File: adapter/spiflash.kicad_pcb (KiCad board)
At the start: 2 copper layers, 35 x 22 mm, 45 parts, among them J1 USB_C_Receptacle_USB2.0, J2 Tag-Connect, J3 Conn_01x02, J4 Conn_01x03, J5 Clip, U1 XC6206, U2 SRV05-4-P-T7, U4 STM32F103C8T6, U5 SN74LVC1T45DBV, U6 SN74LVC1T45DBV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

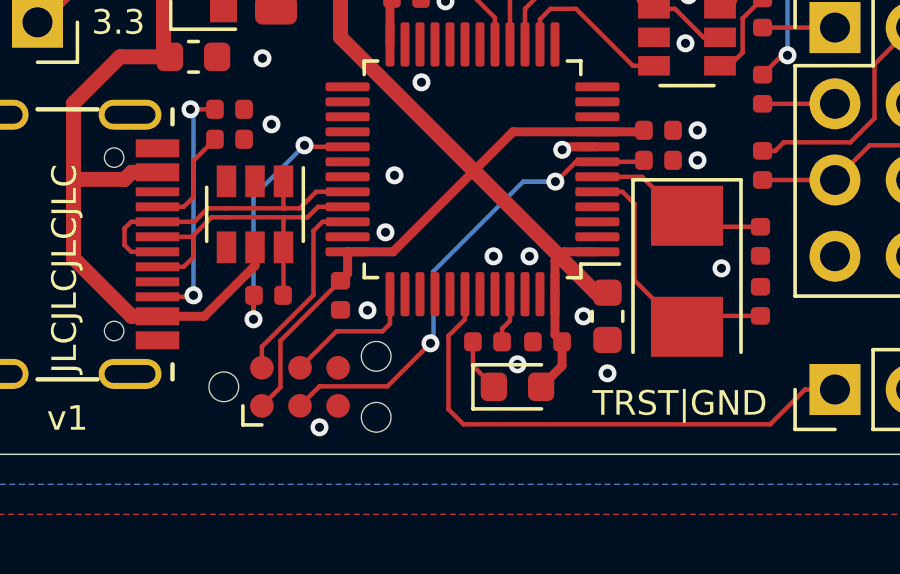
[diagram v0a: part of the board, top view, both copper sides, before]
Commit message: remap TRST
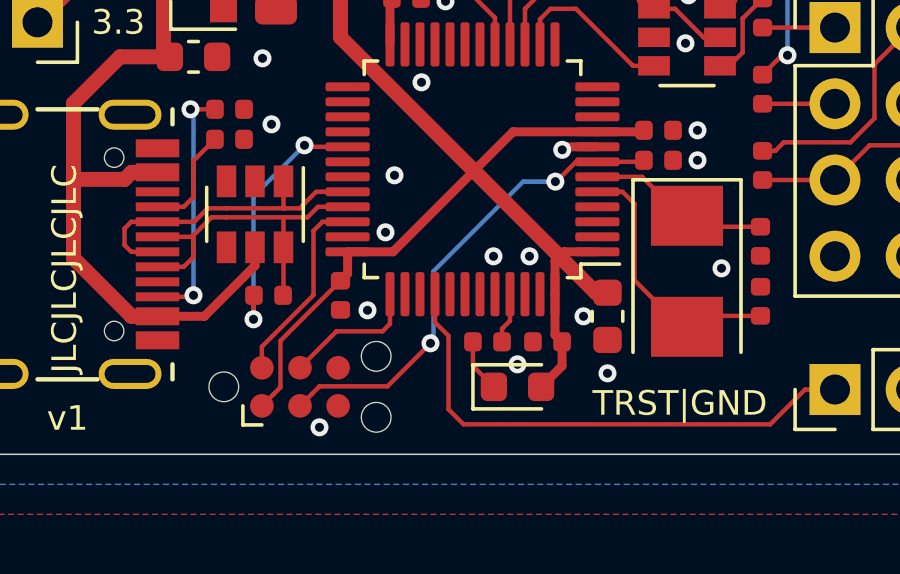
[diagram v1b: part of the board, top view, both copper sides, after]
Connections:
- U4 pad 40: Net-(U4-Pad40) -> /TRST
- U4 pad 42: /TRST -> Net-(U4-Pad42)

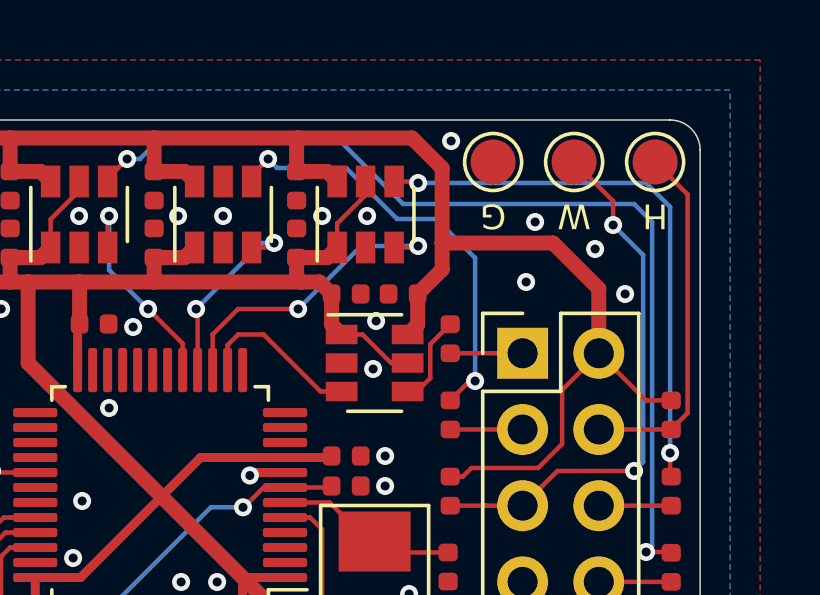
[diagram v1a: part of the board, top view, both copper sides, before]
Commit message: adapter: add Vtarget decoupling
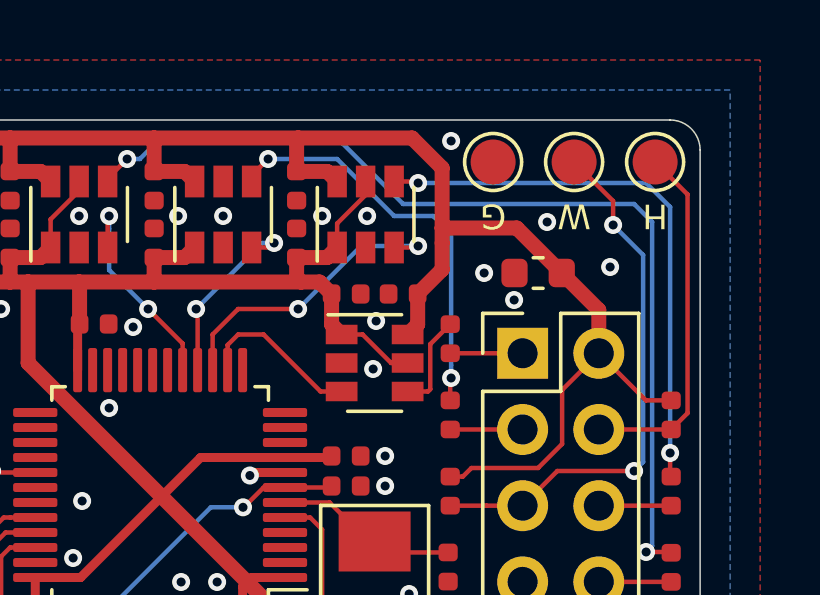
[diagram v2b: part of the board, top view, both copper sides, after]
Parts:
- added C5: 1u, Capacitor_SMD:C_0603_1608Metric, F.Cu at (129.6, 83.1)
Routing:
- net /MISO: track 14.4 -> 13.7 mm
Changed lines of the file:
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@@
     (thickness 1.6)
     (drawings 21)
-    (tracks 329)
+    (tracks 331)
     (zones 0)
-    (modules 45)
+    (modules 46)
     (nets 61)
   )
@@
     (add_net VBUS)
   )
+  (module Capacitor_SMD:C_0603_1608Metric (layer F.Cu)
+    (at 129.6 83.1 180)
+    (descr "Capacitor SMD 0603 (1608 Metric), square (rectangular) end terminal, IPC_7351 nominal, (Body size source: http://www.tortai-tech.com/upload/download/2011102023233369053.pdf), generated with kicad-footprint-generator")
+    (tags capacitor)
+    (attr smd)
+    (fp_text reference C5 (at 0 -1.43) (layer F.SilkS) hide
+      (effects (font (size 1 1) (thickness 0.15)))
+    )
+    (fp_text value 1u (at 0 1.43) (layer F.Fab)
+      (effects (font (size 1 1) (thickness 0.15)))
+    )
+    (fp_text user %R (at 0 0) (layer F.Fab)
+      (effects (font (size 0.4 0.4) (thickness 0.06)))
+    )
+    (fp_line (start 1.48 0.73) (end -1.48 0.73) (layer F.CrtYd) (width 0.05))
+    (fp_line (start 1.48 -0.73) (end 1.48 0.73) (layer F.CrtYd) (width 0.05))
+    (fp_line (start -1.48 -0.73) (end 1.48 -0.73) (layer F.CrtYd) (width 0.05))
+    (fp_line (start -1.48 0.73) (end -1.48 -0.73) (layer F.CrtYd) (width 0.05))
+    (fp_line (start -0.162779 0.51) (end 0.162779 0.51) (layer F.SilkS) (width 0.12))
+    (fp_line (start -0.162779 -0.51) (end 0.162779 -0.51) (layer F.SilkS) (width 0.12))
+    (fp_line (start 0.8 0.4) (end -0.8 0.4) (layer F.Fab) (width 0.1))
+    (fp_line (start 0.8 -0.4) (end 0.8 0.4) (layer F.Fab) (width 0.1))
+    (fp_line (start -0.8 -0.4) (end 0.8 -0.4) (layer F.Fab) (width 0.1))
+    (fp_line (start -0.8 0.4) (end -0.8 -0.4) (layer F.Fab) (width 0.1))
+    (pad 2 smd roundrect (at 0.7875 0 180) (size 0.875 0.95) (layers F.Cu F.Paste F.Mask) (roundrect_rratio 0.25)
+      (net 1 GND))
+    (pad 1 smd roundrect (at -0.7875 0 180) (size 0.875 0.95) (layers F.Cu F.Paste F.Mask) (roundrect_rratio 0.25)
+      (net 6 /V_TARGET))
+    (model ${KISYS3DMOD}/Capacitor_SMD.3dshapes/C_0603_1608Metric.wrl
+      (at (xyz 0 0 0))
+      (scale (xyz 1 1 1))
+      (rotate (xyz 0 0 0))
+    )
+  )
   (module Package_TO_SOT_SMD:SOT-23 (layer F.Cu)
     (at 107.7 84.25 180)
@@
   (via (at 124.5 89.2) (size 0.6) (drill 0.3) (layers F.Cu B.Cu) (net 1))
   (via (at 124.5 90.2) (size 0.6) (drill 0.3) (layers F.Cu B.Cu) (net 1))
-  (via (at 131.5 82.3) (size 0.6) (drill 0.3) (layers F.Cu B.Cu) (net 1))
-  (via (at 132.5 83.8) (size 0.6) (drill 0.3) (layers F.Cu B.Cu) (net 1))
-  (via (at 129.5 81.4) (size 0.6) (drill 0.3) (layers F.Cu B.Cu) (net 1))
-  (via (at 129.2 83.4) (size 0.6) (drill 0.3) (layers F.Cu B.Cu) (net 1))
   (via (at 126.7 78.7) (size 0.6) (drill 0.3) (layers F.Cu B.Cu) (net 1))
   (via (at 121.5 97.3) (size 0.6) (drill 0.3) (layers F.Cu B.Cu) (net 1))
+  (via (at 127.8 83.1) (size 0.6) (drill 0.3) (layers F.Cu B.Cu) (net 1))
+  (via (at 128.8 84) (size 0.6) (drill 0.3) (layers F.Cu B.Cu) (net 1))
+  (via (at 132 82.9) (size 0.6) (drill 0.3) (layers F.Cu B.Cu) (net 1))
+  (via (at 129.9 81.4) (size 0.6) (drill 0.3) (layers F.Cu B.Cu) (net 1))
   (segment (start 106.5 90.6) (end 105.638002 90.6) (width 0.5) (layer F.Cu) (net 2))
   (segment (start 109.75 93.712124) (end 109.75 93.1) (width 0.3) (layer F.Cu) (net 2))
@@
   (segment (start 121.6 78.6) (end 121.55 78.65) (width 0.5) (layer F.Cu) (net 6))
   (segment (start 121.6 78.6) (end 125.4 78.6) (width 0.5) (layer F.Cu) (net 6))
-  (segment (start 126.4 79.6) (end 126.4 82.1) (width 0.5) (layer F.Cu) (net 6))
   (segment (start 126.4 82.1) (end 126.4 82.985) (width 0.5) (layer F.Cu) (net 6))
-  (segment (start 131.623 85.776) (end 131.623 83.623) (width 0.5) (layer F.Cu) (net 6))
-  (segment (start 130.1 82.1) (end 126.4 82.1) (width 0.5) (layer F.Cu) (net 6))
-  (segment (start 131.623 83.623) (end 130.1 82.1) (width 0.5) (layer F.Cu) (net 6))
   (segment (start 130.4 86.999) (end 131.623 85.776) (width 0.15) (layer F.Cu) (net 6))
   (segment (start 127.09 89.886) (end 127.376 89.6) (width 0.15) (layer F.Cu) (net 6))
@@
   (segment (start 129.6 89.6) (end 130.4 88.8) (width 0.15) (layer F.Cu) (net 6))
   (segment (start 130.4 88.8) (end 130.4 86.999) (width 0.15) (layer F.Cu) (net 6))
+  (segment (start 131.623 84.3355) (end 130.3875 83.1) (width 0.5) (layer F.Cu) (net 6))
+  (segment (start 131.623 85.776) (end 131.623 84.3355) (width 0.5) (layer F.Cu) (net 6))
+  (segment (start 128.8875 81.6) (end 126.4 81.6) (width 0.5) (layer F.Cu) (net 6))
+  (segment (start 130.3875 83.1) (end 128.8875 81.6) (width 0.5) (layer F.Cu) (net 6))
+  (segment (start 126.4 79.6) (end 126.4 81.6) (width 0.5) (layer F.Cu) (net 6))
+  (segment (start 126.4 81.6) (end 126.4 82.1) (width 0.5) (layer F.Cu) (net 6))
   (segment (start 123.95 92.05) (end 124.15 92.05) (width 0.15) (layer F.Cu) (net 7))
   (segment (start 122.65 90.75) (end 123.95 92.05) (width 0.15) (layer F.Cu) (net 7))
@@
   (segment (start 118.25 94.6625) (end 118.25 95.55) (width 0.15) (layer F.Cu) (net 25))
   (segment (start 118.25 95.55) (end 117.985 95.815) (width 0.15) (layer F.Cu) (net 25))
-  (segment (start 126.005001 86.605001) (end 125.560002 87.05) (width 0.15) (layer F.Cu) (net 26))
-  (segment (start 125.560002 87.05) (end 125.25 87.05) (width 0.15) (layer F.Cu) (net 26))
+  (segment (start 126.005001 85.470999) (end 126.005001 86.974999) (width 0.15) (layer F.Cu) (net 26))
   (segment (start 126.67 84.806) (end 126.005001 85.470999) (width 0.15) (layer F.Cu) (net 26))
-  (segment (start 126.005001 85.470999) (end 126.005001 86.605001) (width 0.15) (layer F.Cu) (net 26))
+  (segment (start 125.93 87.05) (end 125.25 87.05) (width 0.15) (layer F.Cu) (net 26))
+  (segment (start 126.005001 86.974999) (end 125.93 87.05) (width 0.15) (layer F.Cu) (net 26))
   (via (at 120.6 79.3) (size 0.6) (drill 0.3) (layers F.Cu B.Cu) (net 27))
   (segment (start 120.05 80.05) (end 120.05 79.85) (width 0.15) (layer F.Cu) (net 27))
   (segment (start 120.05 79.85) (end 120.6 79.3) (width 0.15) (layer F.Cu) (net 27))
-  (segment (start 120.899999 79.599999) (end 123.199999 79.599999) (width 0.15) (layer B.Cu) (net 27))
-  (segment (start 120.6 79.3) (end 120.899999 79.599999) (width 0.15) (layer B.Cu) (net 27))
-  (segment (start 123.199999 79.599999) (end 124.9 81.3) (width 0.15) (layer B.Cu) (net 27))
-  (segment (start 124.9 81.3) (end 126.2 81.3) (width 0.15) (layer B.Cu) (net 27))
-  (segment (start 126.2 81.3) (end 127.5 82.6) (width 0.15) (layer B.Cu) (net 27))
-  (via (at 127.5 86.7) (size 0.6) (drill 0.3) (layers F.Cu B.Cu) (net 27))
-  (segment (start 127.5 82.6) (end 127.5 86.7) (width 0.15) (layer B.Cu) (net 27))
-  (segment (start 127.316 86.7) (end 126.67 87.346) (width 0.15) (layer F.Cu) (net 27))
-  (segment (start 127.5 86.7) (end 127.316 86.7) (width 0.15) (layer F.Cu) (net 27))
+  (segment (start 126.1 81.2) (end 126.7 81.8) (width 0.15) (layer B.Cu) (net 27))
+  (segment (start 122.9 79.3) (end 124.8 81.2) (width 0.15) (layer B.Cu) (net 27))
+  (segment (start 124.8 81.2) (end 126.1 81.2) (width 0.15) (layer B.Cu) (net 27))
+  (segment (start 120.6 79.3) (end 122.9 79.3) (width 0.15) (layer B.Cu) (net 27))
+  (segment (start 126.7 86.175736) (end 126.7 86.6) (width 0.15) (layer B.Cu) (net 27))
+  (segment (start 126.7 81.8) (end 126.7 86.175736) (width 0.15) (layer B.Cu) (net 27))
+  (segment (start 126.67 87.346) (end 126.67 86.63) (width 0.15) (layer F.Cu) (net 27))
+  (segment (start 126.67 86.63) (end 126.7 86.6) (width 0.15) (layer F.Cu) (net 27))
+  (via (at 126.7 86.6) (size 0.6) (drill 0.3) (layers F.Cu B.Cu) (net 27))
   (via (at 111.4 89.7) (size 0.6) (drill 0.3) (layers F.Cu B.Cu) (net 28))
   (segment (start 112.8375 89.75) (end 111.45 89.75) (width 0.15) (layer F.Cu) (net 28))
